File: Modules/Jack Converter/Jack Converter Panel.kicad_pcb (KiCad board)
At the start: 2 copper layers, 50 x 200 mm, 6 parts

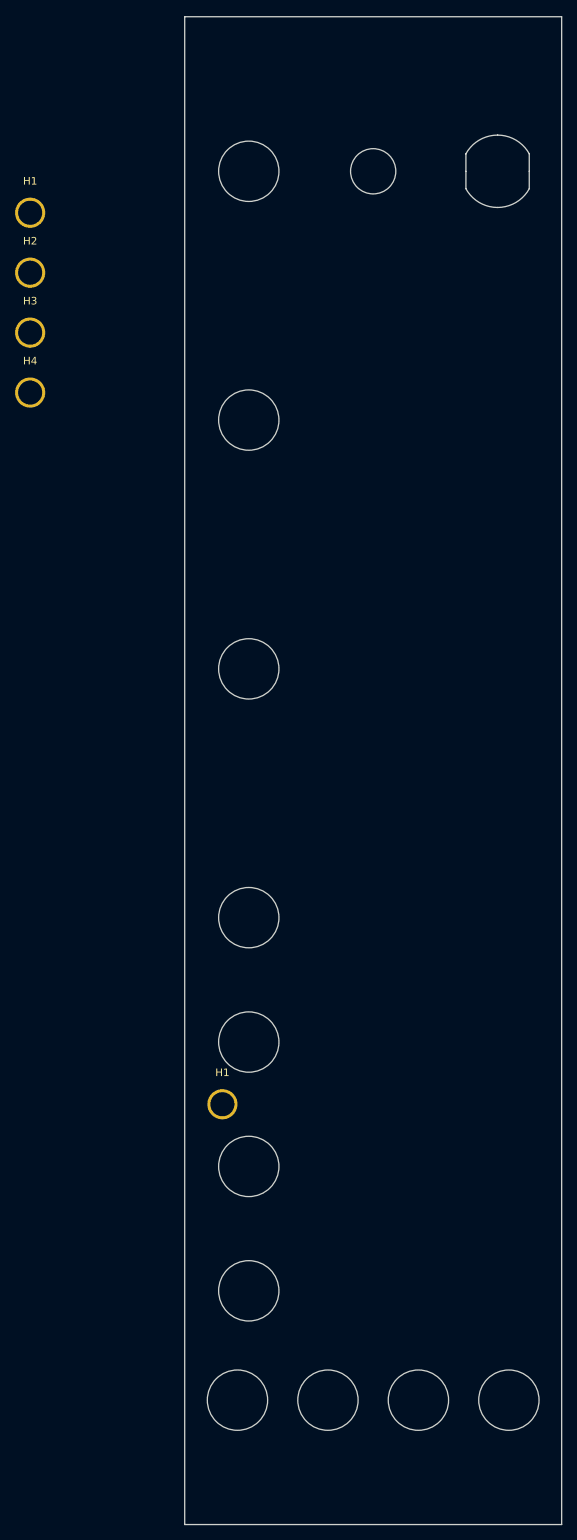
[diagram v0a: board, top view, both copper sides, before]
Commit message: Front panel design ongoing
Deleted spacer hole, positioned all holes, started decals
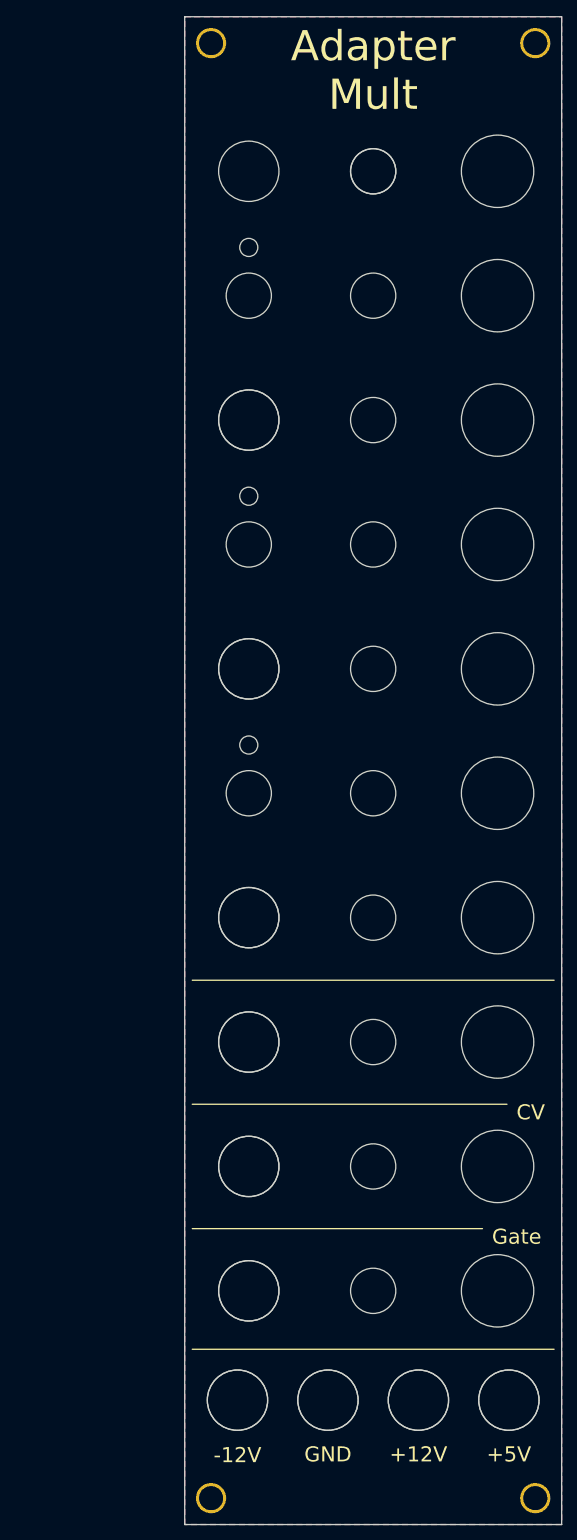
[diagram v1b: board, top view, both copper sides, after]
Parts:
- removed the H1 at (83.0, 192.8)
- removed REF**: Banana_Jack_Cutout, SynthStuff:Banana_Jack_Cutout
- added H10: MountingHole_Jack3.5mm, SynthStuff:Jack_3.5mm_Cutout, F.Cu at (103.0, 85.5)
- added H11: MountingHole_Jack6.35mm, SynthStuff:Jack_6.35mm_Cutout, F.Cu at (119.5, 85.5)
- added H12: MountingHole_BananaJack, SynthStuff:Banana_Jack_Cutout, F.Cu at (86.5, 102.0)
- added H13: MountingHole_Jack3.5mm, SynthStuff:Jack_3.5mm_Cutout, F.Cu at (103.0, 102.0)
- added H14: MountingHole_Jack6.35mm, SynthStuff:Jack_6.35mm_Cutout, F.Cu at (119.5, 102.0)
- added H15: MountingHole_ToggleSwitch, SynthStuff:Toggle_Switch_Cutout, F.Cu at (86.5, 118.5)
- added H16: MountingHole_Jack3.5mm, SynthStuff:Jack_3.5mm_Cutout, F.Cu at (103.0, 118.5)
- added H17: MountingHole_Jack6.35mm, SynthStuff:Jack_6.35mm_Cutout, F.Cu at (119.5, 118.5)
- added H18: MountingHole_BananaJack, SynthStuff:Banana_Jack_Cutout, F.Cu at (86.5, 135.0)
- added H19: MountingHole_Jack3.5mm, SynthStuff:Jack_3.5mm_Cutout, F.Cu at (103.0, 135.0)
- added H20: MountingHole_Jack6.35mm, SynthStuff:Jack_6.35mm_Cutout, F.Cu at (119.5, 135.0)
- added H21: MountingHole_ToggleSwitch, SynthStuff:Toggle_Switch_Cutout, F.Cu at (86.5, 151.5)
- added H22: MountingHole_Jack3.5mm, SynthStuff:Jack_3.5mm_Cutout, F.Cu at (103.0, 151.5)
- added H23: MountingHole_Jack6.35mm, SynthStuff:Jack_6.35mm_Cutout, F.Cu at (119.5, 151.5)
- added H24: MountingHole_BananaJack, SynthStuff:Banana_Jack_Cutout, F.Cu at (86.5, 168.0)
- added H25: MountingHole_Jack3.5mm, SynthStuff:Jack_3.5mm_Cutout, F.Cu at (103.0, 168.0)
- added H26: MountingHole_Jack6.35mm, SynthStuff:Jack_6.35mm_Cutout, F.Cu at (119.5, 168.0)
- added H27: MountingHole_BananaJack, SynthStuff:Banana_Jack_Cutout, F.Cu at (86.5, 184.5)
- added H28: MountingHole_Jack3.5mm, SynthStuff:Jack_3.5mm_Cutout, F.Cu at (103.0, 184.5)
- added H29: MountingHole_Jack6.35mm, SynthStuff:Jack_6.35mm_Cutout, F.Cu at (119.5, 184.5)
- added H30: Banana_CV, SynthStuff:Banana_Jack_Cutout, F.Cu at (86.5, 201.0)
- added H31: Jack3.5mm_CV, SynthStuff:Jack_3.5mm_Cutout, F.Cu at (103.0, 201.0)
- added H32: Jack6.35mm_CV, SynthStuff:Jack_6.35mm_Cutout, F.Cu at (119.5, 201.0)
- added H33: Banana_Gate, SynthStuff:Banana_Jack_Cutout, F.Cu at (86.5, 217.5)
- added H34: Jack3.5mm_Gate, SynthStuff:Jack_3.5mm_Cutout, F.Cu at (103.0, 217.5)
- added H35: Jack6.35mm_Gate, SynthStuff:Jack_6.35mm_Cutout, F.Cu at (119.5, 217.5)
- added H36: Banana_-12V, SynthStuff:Banana_Jack_Cutout, F.Cu at (85.0, 232.0)
- added H37: Banana_GND, SynthStuff:Banana_Jack_Cutout, F.Cu at (97.0, 232.0)
- added H38: Banana_+12V, SynthStuff:Banana_Jack_Cutout, F.Cu at (109.0, 232.0)
- added H39: Banana_+5V, SynthStuff:Banana_Jack_Cutout, F.Cu at (121.0, 232.0)
- added H6: MountingHole_BananaJack, SynthStuff:Banana_Jack_Cutout, F.Cu at (86.5, 69.0)
- added H7: MountingHole_Jack3.5mm, SynthStuff:Jack_3.5mm_Cutout, F.Cu at (103.0, 69.0)
- added H8: MountingHole_Jack6.35mm, SynthStuff:Jack_6.35mm_Cutout, F.Cu at (119.5, 69.0)
- added H9: MountingHole_ToggleSwitch, SynthStuff:Toggle_Switch_Cutout, F.Cu at (86.5, 85.5)
- H1, H2, H3, H4: value MountingHole_Pad -> MountingHole_Rails
- moved H4 161.2 mm to (124.5, 245.0)
- moved H3 156.5 mm to (81.5, 245.0)
- moved H2 73.6 mm to (124.5, 52.0)
- moved H1 32.9 mm to (81.5, 52.0)
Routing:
- added copper zone on B.Cu, net GND
- added copper zone on F.Cu, net GND
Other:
- outline, holes or cut-outs redrawn
- board text added: "+12V"
- board text added: "+5V"
- board text added: "-12V"
- board text added: "Adapter Mult"
- board text added: "CV"
- board text added: "GND"
- board text added: "Gate"
- board text added: "JLCJLCJLCJLC"
- board text added: "Mk1 - May 2024"
